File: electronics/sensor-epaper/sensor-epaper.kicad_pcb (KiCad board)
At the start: 4 copper layers, 34 x 79.2 mm, 92 parts, among them J1 i2c, J2 Conn_01x06, J4 Display, J9 USB micro, Q1 Q_NMOS_GSD, Q2 NX2301P, Q3 NX2301P, SW1 SW_Push, U1 ESP32-C3FN4, U2 AMS1117-3.3, U4 SHT40-AD1B-R2, U5 TPS61023, Y2 32kHz, Y3 40MHz 10ppm

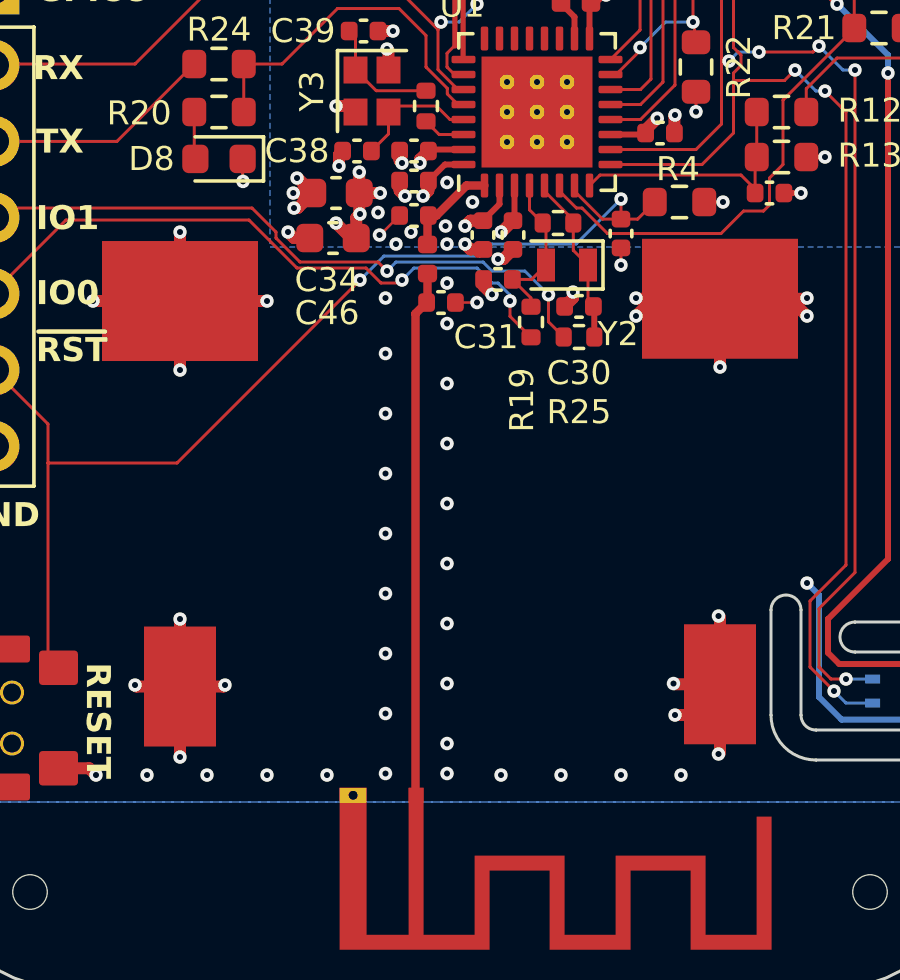
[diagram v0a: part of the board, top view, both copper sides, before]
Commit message: Fix antenna trace so it's 50 Ohm
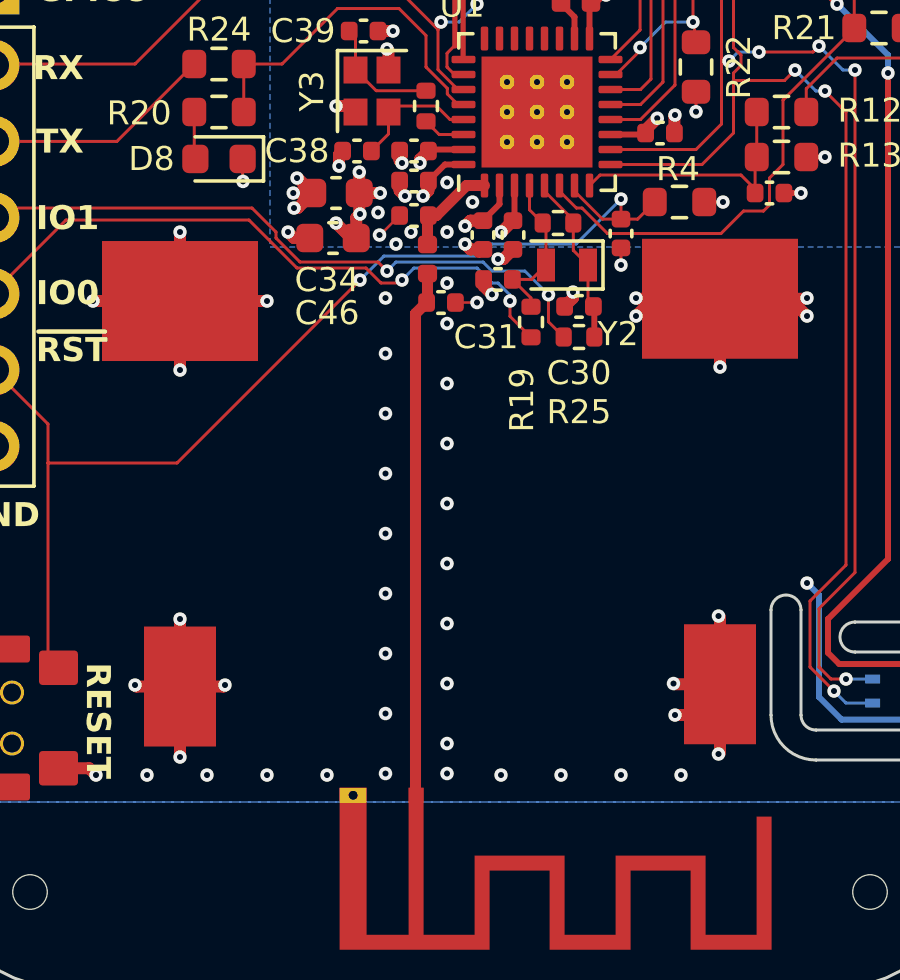
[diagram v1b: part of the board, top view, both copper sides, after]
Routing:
- net GND: vias 188 -> 187
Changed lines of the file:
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@@
   (via (at 193.4 67.2) (size 0.45) (drill 0.2) (layers "F.Cu" "B.Cu") (remove_unused_layers) (keep_end_layers) (zone_layer_connections "In1.Cu" "In2.Cu") (net 1))
   (via (at 196.3 48.1) (size 0.45) (drill 0.2) (layers "F.Cu" "B.Cu") (remove_unused_layers) (keep_end_layers) (zone_layer_connections "In1.Cu" "In2.Cu") (net 1))
-  (via (at 182.85 90.8) (size 0.45) (drill 0.2) (layers "F.Cu" "B.Cu") (remove_unused_layers) (keep_end_layers) (free) (zone_layer_connections "In1.Cu" "In2.Cu") (net 1))
   (via (at 174.9 109.1) (size 0.45) (drill 0.2) (layers "F.Cu" "B.Cu") (remove_unused_layers) (keep_end_layers) (zone_layer_connections "In1.Cu" "In2.Cu") (net 1))
   (via (at 175.5 38.6) (size 0.45) (drill 0.2) (layers "F.Cu" "B.Cu") (remove_unused_layers) (keep_end_layers) (free) (zone_layer_connections "In1.Cu" "In2.Cu") (net 1))
@@
   (via (at 197 39.9) (size 0.45) (drill 0.2) (layers "F.Cu" "B.Cu") (remove_unused_layers) (keep_end_layers) (free) (zone_layer_connections "In1.Cu" "In2.Cu") (net 1))
   (via (at 184.4 76.55) (size 0.45) (drill 0.2) (layers "F.Cu" "B.Cu") (net 1))
-  (via (at 182.9 91.4) (size 0.45) (drill 0.2) (layers "F.Cu" "B.Cu") (remove_unused_layers) (keep_end_layers) (zone_layer_connections "In1.Cu" "In2.Cu") (net 1))
+  (via (at 182.9 91) (size 0.45) (drill 0.2) (layers "F.Cu" "B.Cu") (remove_unused_layers) (keep_end_layers) (zone_layer_connections "In1.Cu" "In2.Cu") (net 1))
   (via (at 191.2 71.1) (size 0.45) (drill 0.2) (layers "F.Cu" "B.Cu") (remove_unused_layers) (keep_end_layers) (zone_layer_connections "In1.Cu" "In2.Cu") (net 1))
   (via (at 195.5 88.5) (size 0.45) (drill 0.2) (layers "F.Cu" "B.Cu") (remove_unused_layers) (keep_end_layers) (zone_layer_connections "In1.Cu" "In2.Cu") (net 1))
@@
   (segment (start 188 89.1) (end 187.65 89.45) (width 0.1) (layer "F.Cu") (net 28))
   (segment (start 174.475 87) (end 174.475 88.6) (width 0.1) (layer "F.Cu") (net 29))
-  (segment (start 183.55 89.45) (end 182.55 90.45) (width 0.283) (layer "F.Cu") (net 31))
-  (segment (start 182.55 90.45) (end 182.28 90.45) (width 0.283) (layer "F.Cu") (net 31))
-  (segment (start 182.25 90.48) (end 182.25 91.415) (width 0.283) (layer "F.Cu") (net 31))
-  (segment (start 184.15 89.45) (end 183.55 89.45) (width 0.283) (layer "F.Cu") (net 31))
-  (segment (start 182.22 93.35) (end 181.85 93.72) (width 0.283) (layer "F.Cu") (net 32))
-  (segment (start 182.25 92.385) (end 182.25 93.32) (width 0.283) (layer "F.Cu") (net 32))
-  (segment (start 181.85 93.72) (end 181.85 109.755) (width 0.283) (layer "F.Cu") (net 32))
+  (segment (start 183.55 89.45) (end 182.55 90.45) (width 0.368466) (layer "F.Cu") (net 31))
+  (segment (start 182.55 90.45) (end 182.28 90.45) (width 0.368466) (layer "F.Cu") (net 31))
+  (segment (start 182.25 90.48) (end 182.25 91.415) (width 0.368466) (layer "F.Cu") (net 31))
+  (segment (start 184.15 89.45) (end 183.55 89.45) (width 0.368466) (layer "F.Cu") (net 31))
+  (segment (start 182.22 93.35) (end 181.85 93.72) (width 0.368466) (layer "F.Cu") (net 32))
+  (segment (start 182.25 92.385) (end 182.25 93.32) (width 0.368466) (layer "F.Cu") (net 32))
+  (segment (start 181.85 93.72) (end 181.85 109.755) (width 0.368466) (layer "F.Cu") (net 32))
   (segment (start 176.125 85.4) (end 176.125 87) (width 0.1) (layer "F.Cu") (net 33))
   (segment (start 179.25 83.55) (end 181.3 83.55) (width 0.1) (layer "F.Cu") (net 33))
@@
   )
   (zone (net 49) (net_name "/SW_MAIN") (layer "F.Cu") (hatch edge 0.508)
-    (priority 3)
+    (priority 5)
     (connect_pads yes (clearance 0.2))
     (min_thickness 0.2) (filled_areas_thickness no)
